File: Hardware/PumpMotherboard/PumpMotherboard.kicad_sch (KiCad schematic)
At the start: 1 part

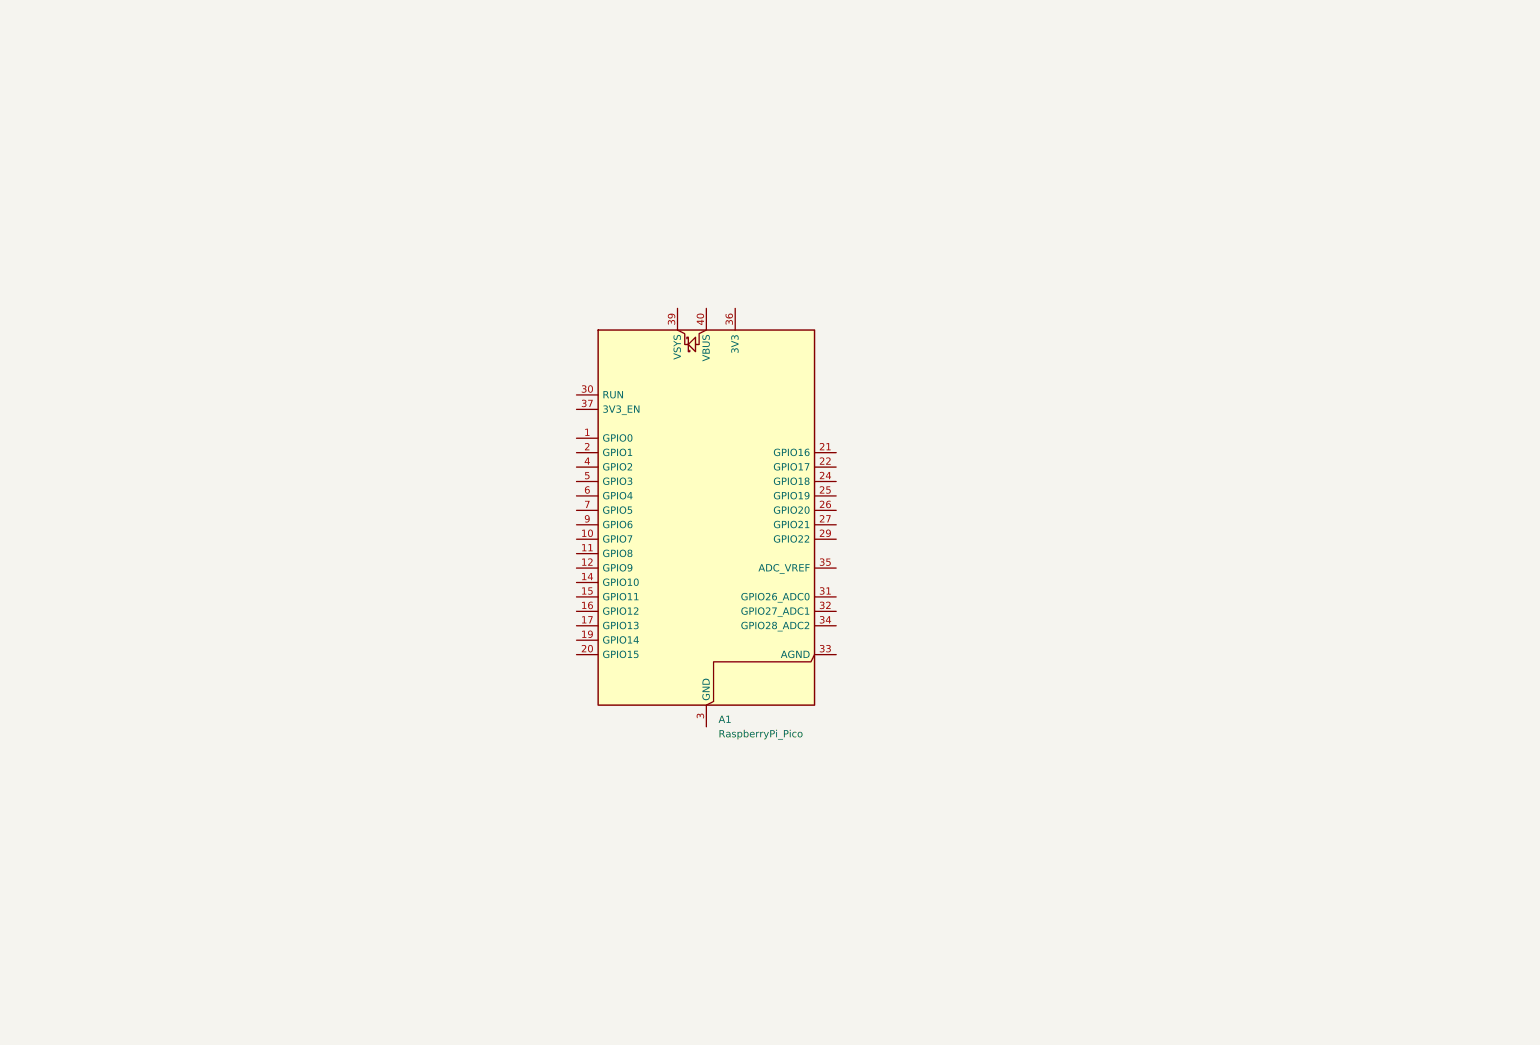
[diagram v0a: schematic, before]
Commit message: Add more bits to motherboard/controller panel
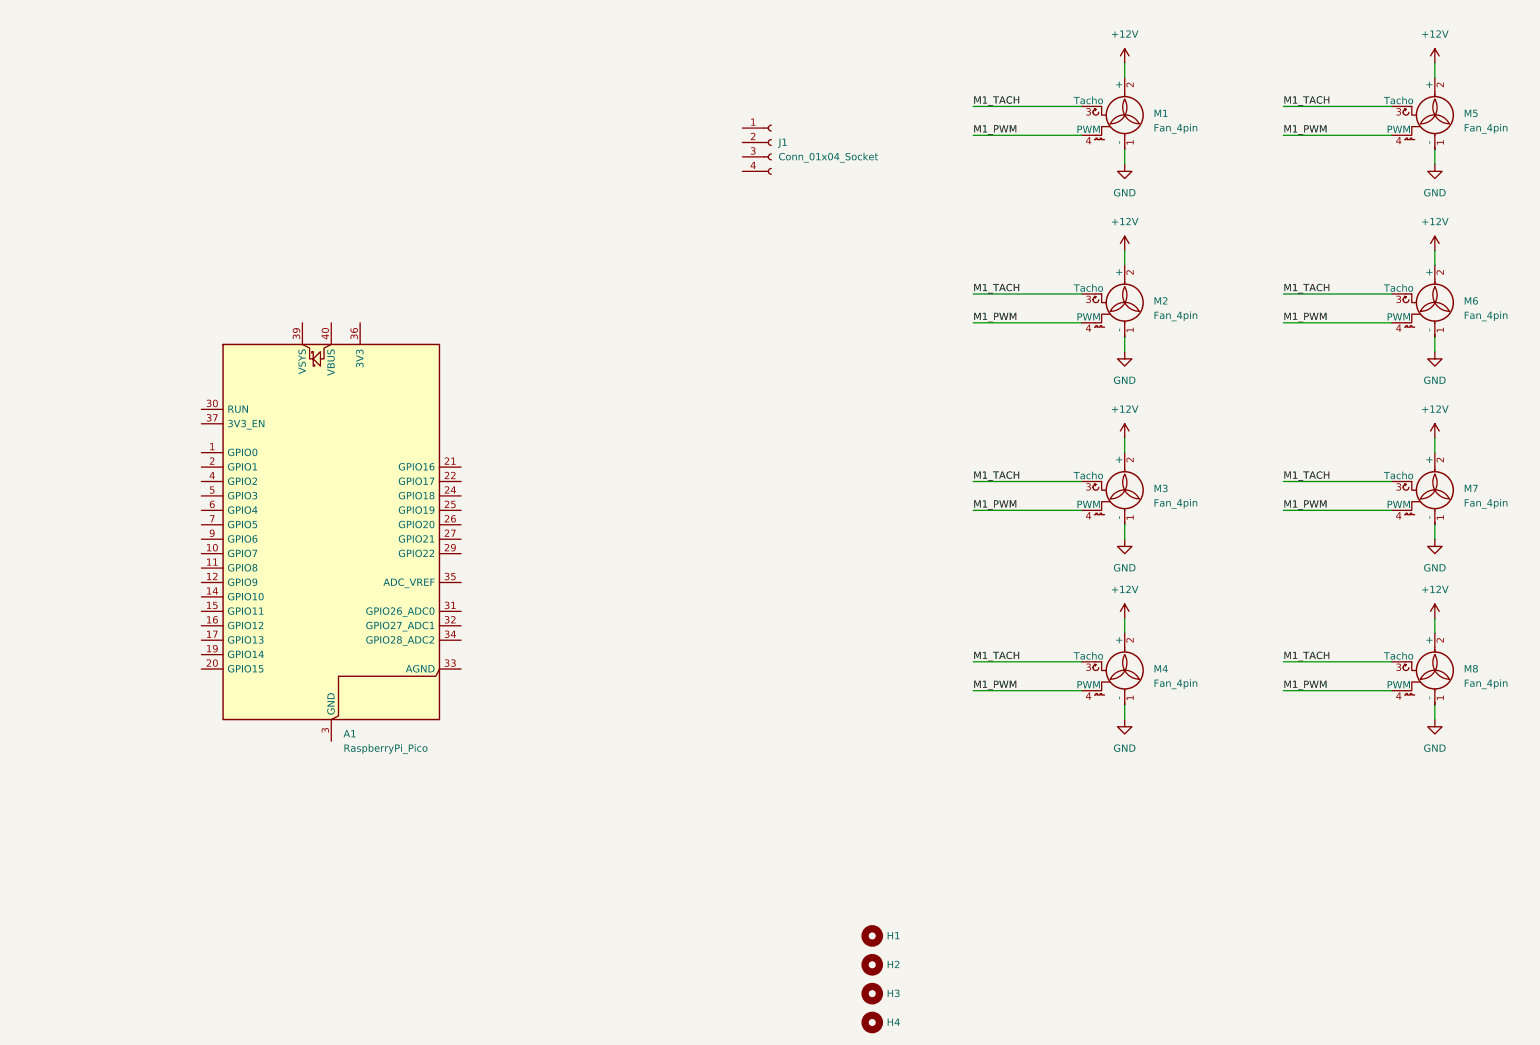
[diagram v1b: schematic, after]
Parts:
- added H1, H2, H3, H4: MountingHole, MountingHole:MountingHole_4.3mm_M4, symbol Mechanical:MountingHole
- added J1: Conn_01x04_Socket, Connector_PinSocket_2.54mm:PinSocket_1x04_P2.54mm_Vertical, symbol Connector:Conn_01x04_Socket
- added M1, M2, M3, M4, M5, M6, M7, M8: Fan_4pin, Connector:FanPinHeader_1x04_P2.54mm_Vertical, symbol Motor:Fan_4pin
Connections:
- new net +12V: M1.2 (+), M2.2 (+), M3.2 (+), M4.2 (+), M5.2 (+), M6.2 (+), M7.2 (+), M8.2 (+)
- new net GND: M1.1 (-), M2.1 (-), M3.1 (-), M4.1 (-), M5.1 (-), M6.1 (-), M7.1 (-), M8.1 (-)
- new net M1_PWM: M1.4 (PWM), M2.4 (PWM), M3.4 (PWM), M4.4 (PWM), M5.4 (PWM), M6.4 (PWM), M7.4 (PWM), M8.4 (PWM)
- new net M1_TACH: M1.3 (Tacho), M2.3 (Tacho), M3.3 (Tacho), M4.3 (Tacho), M5.3 (Tacho), M6.3 (Tacho), M7.3 (Tacho), M8.3 (Tacho)
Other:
- moved on the sheet: A1

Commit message: Replicate plugin is being a pain
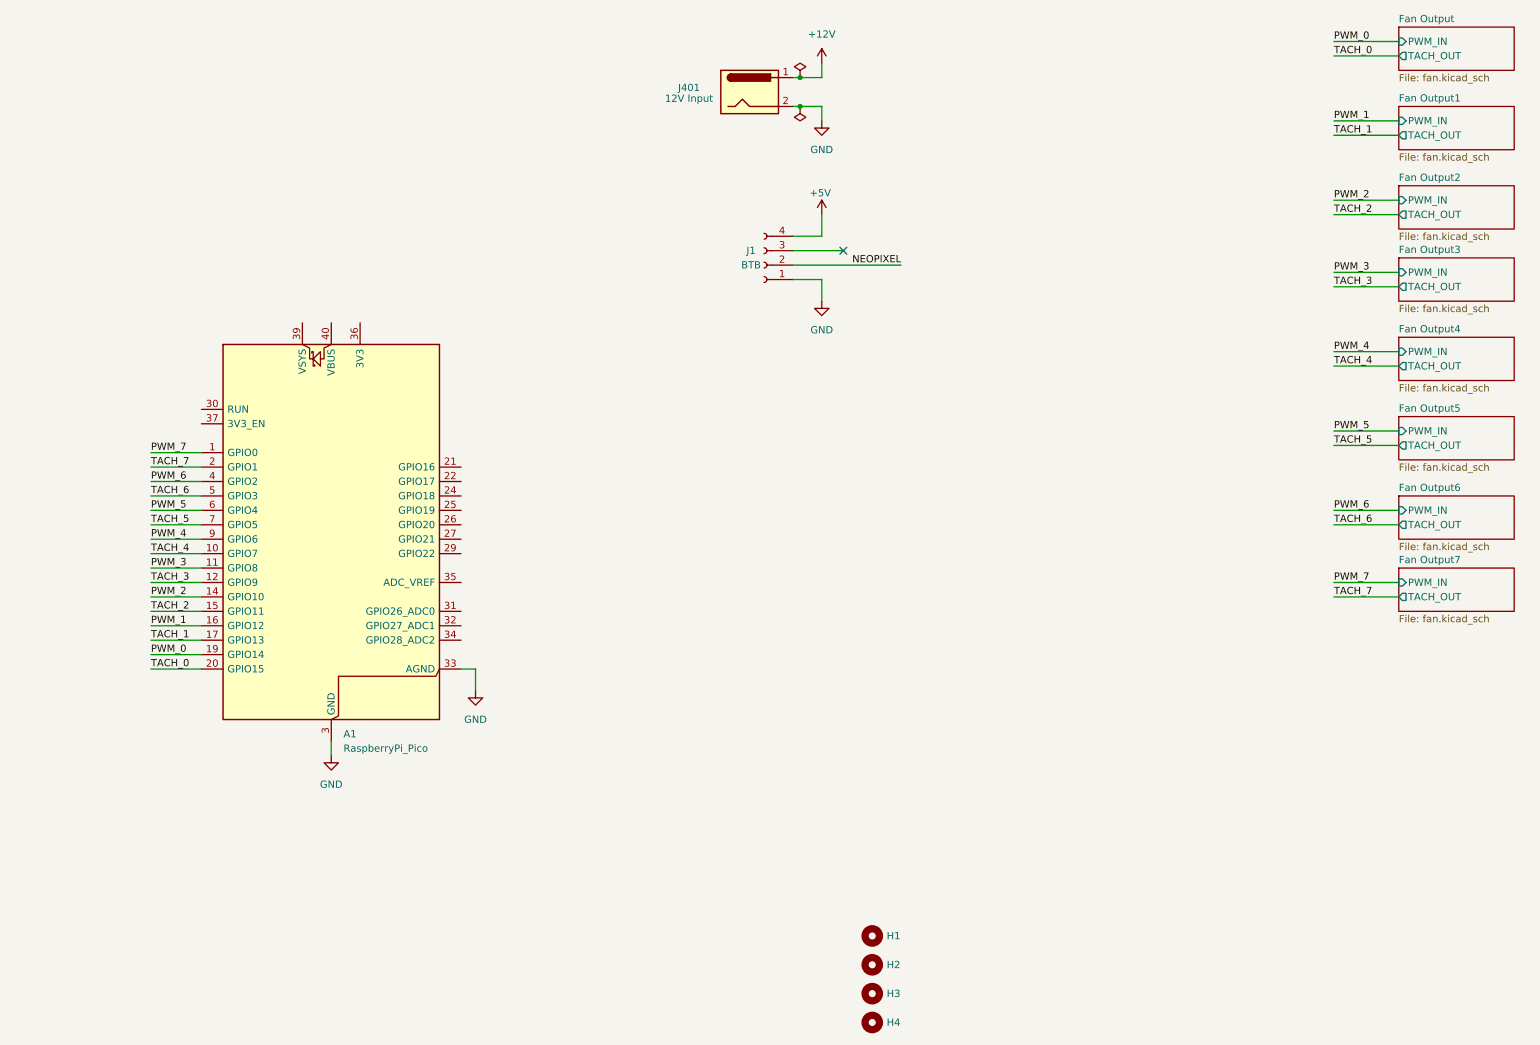
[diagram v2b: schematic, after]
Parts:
- removed M1, M2, M3, M4, M5, M6, M7, M8: Fan_4pin, Connector:FanPinHeader_1x04_P2.54mm_Vertical, symbol Motor:Fan_4pin
- added J401: 12V Input, Connector_BarrelJack:BarrelJack_GCT_DCJ200-10-A_Horizontal, symbol Connector:Barrel_Jack
- J1: value Conn_01x04_Socket -> BTB
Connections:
- net +12V: now also J401.1
- net GND: now also A1.13 (GND), A1.18 (GND), A1.23 (GND), A1.28 (GND), A1.3 (GND), A1.33 (AGND), A1.38 (GND), A1.8 (GND), J1.1 (Pin_1), J401.2
- net PWM_7: now reaches A1.1 (GPIO0)
- net TACH_4: now reaches A1.10 (GPIO7)
- net PWM_3: now reaches A1.11 (GPIO8)
- net TACH_3: now reaches A1.12 (GPIO9)
- net PWM_2: now reaches A1.14 (GPIO10)
- net TACH_2: now reaches A1.15 (GPIO11)
- net PWM_1: now reaches A1.16 (GPIO12)
- net TACH_1: now reaches A1.17 (GPIO13)
- net PWM_0: now reaches A1.19 (GPIO14)
- net TACH_7: now reaches A1.2 (GPIO1)
- net TACH_0: now reaches A1.20 (GPIO15)
- net PWM_6: now reaches A1.4 (GPIO2)
- net TACH_6: now reaches A1.5 (GPIO3)
- net PWM_5: now reaches A1.6 (GPIO4)
- net TACH_5: now reaches A1.7 (GPIO5)
- net PWM_4: now reaches A1.9 (GPIO6)
- net NEOPIXEL: now reaches J1.2 (Pin_2)
- net +5V: now reaches J1.4 (Pin_4)
- no-connect marks 0 -> 1
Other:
- added sheet Fan Output (fan.kicad_sch)
- added sheet Fan Output1 (fan.kicad_sch)
- added sheet Fan Output2 (fan.kicad_sch)
- added sheet Fan Output3 (fan.kicad_sch)
- added sheet Fan Output4 (fan.kicad_sch)
- added sheet Fan Output5 (fan.kicad_sch)
- added sheet Fan Output6 (fan.kicad_sch)
- added sheet Fan Output7 (fan.kicad_sch)
- moved on the sheet: J1

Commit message: Add tsensors, misc bits
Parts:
- added C1: 10uF, Capacitor_SMD:CP_Elec_4x3, symbol Device:C_Polarized
- added C2: 100nF, Capacitor_SMD:C_0805_2012Metric, symbol Device:C_Small
- added D1: PWR, LED_SMD:LED_0805_2012Metric, symbol Device:LED
- added J2: Conn_01x03_Pin, Connector_JST:JST_PH_B3B-PH-K_1x03_P2.00mm_Vertical, symbol Connector:Conn_01x03_Pin
- added L1: 4.7uH, Inductor_SMD:L_APV_ANR4012, symbol Device:L_Small
- added R17: 0R, Resistor_SMD:R_0805_2012Metric, symbol Device:R
- added R18: 1K, Resistor_SMD:R_0805_2012Metric, symbol Device:R
- added U2: AP63205WU, Package_TO_SOT_SMD:TSOT-23-6, symbol Regulator_Switching:AP63205WU
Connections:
- net +12V: now also C1.1, U2.2 (EN), U2.3 (IN)
- net +5V: now also J2.3 (Pin_3), L1.2, R18.1, U2.1 (FB)
- net GND: now also C1.2, D1.1 (K), J2.1 (Pin_1), U2.4 (GND)
- net NEOPIXEL: now also R17.2
- net at A1.21 (GPIO16): now also R17.1
- net AC_LEDS: now reaches A1.22 (GPIO17)
- net AC_LEDS: now also J2.2 (Pin_2)
- net TSENSOR_0: now reaches A1.31 (GPIO26_ADC0)
- net TSENSOR_1: now reaches A1.32 (GPIO27_ADC1)
- net TSENSOR_2: now reaches A1.34 (GPIO28_ADC2)
- net +3V3: now reaches A1.36 (3V3)
- new net: D1.2 (A), R18.2
- new net: C2.2, L1.1, U2.5 (SW)
- new net: C2.1, U2.6 (BST)
- no-connect marks 1 -> 8
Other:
- added sheet NTC Sensor (ntc.kicad_sch)
- added sheet NTC Sensor1 (ntc.kicad_sch)
- added sheet NTC Sensor2 (ntc.kicad_sch)
- moved on the sheet: A1, J1, J401

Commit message: Fix DRC and ERC and add AGND
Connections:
- net +5V: now also A1.39 (VSYS)
- net GND: no longer A1.33 (AGND)
- new net GNDA: A1.33 (AGND)
- no-connect marks 8 -> 10
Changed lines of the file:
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@@
 	)
 	(junction
-		(at 224.79 31.75)
-		(diameter 0)
-		(color 0 0 0 0)
-	)
-	(junction
 		(at 105.41 52.07)
 		(diameter 0)
@@
 	)
 	(no_connect
+		(at 107.95 118.11)
+	)
+	(no_connect
 		(at 153.67 138.43)
 	)
@@
 	)
 	(no_connect
+		(at 107.95 115.57)
+	)
+	(no_connect
 		(at 153.67 130.81)
 	)
@@
 	(wire
 		(pts
-			(xy 224.79 31.75) (xy 223.52 31.75)
-		)
-		(stroke
-			(width 0)
-			(type default)
-		)
-	)
-	(wire
-		(pts
 			(xy 250.19 63.5) (xy 261.62 63.5)
 		)
@@
 	(wire
 		(pts
-			(xy 228.6 31.75) (xy 224.79 31.75)
+			(xy 223.52 31.75) (xy 228.6 31.75)
 		)
 		(stroke
@@
 	(wire
 		(pts
-			(xy 156.21 161.29) (xy 156.21 165.1)
-		)
-		(stroke
-			(width 0)
-			(type default)
-		)
-	)
-	(wire
-		(pts
 			(xy 101.6 52.07) (xy 105.41 52.07)
 		)
@@
 	(wire
 		(pts
-			(xy 156.21 161.29) (xy 153.67 161.29)
-		)
-		(stroke
-			(width 0)
-			(type default)
-		)
-	)
-	(wire
-		(pts
 			(xy 115.57 46.99) (xy 115.57 52.07)
 		)
@@
 	(wire
 		(pts
+			(xy 160.02 161.29) (xy 153.67 161.29)
+		)
+		(stroke
+			(width 0)
+			(type default)
+		)
+	)
+	(wire
+		(pts
+			(xy 160.02 176.53) (xy 160.02 161.29)
+		)
+		(stroke
+			(width 0)
+			(type default)
+		)
+	)
+	(wire
+		(pts
 			(xy 99.06 153.67) (xy 107.95 153.67)
 		)
@@
 	)
 	(symbol
+		(lib_id "power:+5V")
+		(at 125.73 96.52 0)
+		(unit 1)
+		(body_style 1)
+		(exclude_from_sim no)
+		(in_bom yes)
+		(on_board yes)
+		(in_pos_files yes)
+		(dnp no)
+		(fields_autoplaced yes)
+		(property "Reference" "#PWR053"
+			(at 125.73 100.33 0)
+			(hide yes)
+			(show_name no)
+			(do_not_autoplace no)
+			(effects
+				(font
+					(size 1.27 1.27)
+				)
+			)
+		)
+		(property "Value" "+5V"
+			(at 125.73 91.44 0)
+			(show_name no)
+			(do_not_autoplace no)
+			(effects
+				(font
+					(size 1.27 1.27)
+				)
+			)
+		)
+		(property "Footprint" ""
+			(at 125.73 96.52 0)
+			(hide yes)
+			(show_name no)
+			(do_not_autoplace no)
+			(effects
+				(font
+					(size 1.27 1.27)
+				)
+			)
+		)
+		(property "Datasheet" ""
+			(at 125.73 96.52 0)
+			(hide yes)
+			(show_name no)
+			(do_not_autoplace no)
+			(effects
+				(font
+					(size 1.27 1.27)
+				)
+			)
+		)
+		(property "Description" "Power symbol creates a global label with name \"+5V\""
+			(at 125.73 96.52 0)
+			(hide yes)
+			(show_name no)
+			(do_not_autoplace no)
+			(effects
+				(font
+					(size 1.27 1.27)
+				)
+			)
+		)
+		(pin "1"
+		)
+		(instances
+			(project "PumpMotherboard"
+				(path "/0d3b5c69-c1f2-4eab-9f51-de1d9dac9894"
+					(reference "#PWR053")
+					(unit 1)
+				)
+			)
+		)
+	)
+	(symbol
 		(lib_id "Device:C_Polarized")
 		(at 40.64 55.88 0)
@@
 	)
 	(symbol
-		(lib_id "power:PWR_FLAG")
-		(at 224.79 31.75 180)
+		(lib_id "power:GNDA")
+		(at 160.02 176.53 0)
 		(unit 1)
 		(body_style 1)
@@
 		(dnp no)
 		(fields_autoplaced yes)
-		(property "Reference" "#FLG02"
-			(at 224.79 33.655 0)
+		(property "Reference" "#PWR018"
+			(at 160.02 182.88 0)
 			(hide yes)
 			(show_name no)
@@
 			)
 		)
-		(property "Value" "PWR_FLAG"
-			(at 224.79 36.83 0)
-			(hide yes)
+		(property "Value" "GNDA"
+			(at 160.02 181.61 0)
 			(show_name no)
 			(do_not_autoplace no)
@@
 		)
 		(property "Footprint" ""
-			(at 224.79 31.75 0)
+			(at 160.02 176.53 0)
 			(hide yes)
 			(show_name no)
@@
 		)
 		(property "Datasheet" ""
-			(at 224.79 31.75 0)
+			(at 160.02 176.53 0)
 			(hide yes)
 			(show_name no)
@@
 			)
 		)
-		(property "Description" "Special symbol for telling ERC where power comes from"
-			(at 224.79 31.75 0)
+		(property "Description" "Power symbol creates a global label with name \"GNDA\" , analog ground"
+			(at 160.02 176.53 0)
 			(hide yes)
 			(show_name no)
@@
 			(project "PumpMotherboard"
 				(path "/0d3b5c69-c1f2-4eab-9f51-de1d9dac9894"
-					(reference "#FLG02")
+					(reference "#PWR018")
 					(unit 1)
 				)
@@
 	)
 	(symbol
-		(lib_id "power:GND")
-		(at 156.21 165.1 0)
-		(unit 1)
-		(body_style 1)
-		(exclude_from_sim no)
-		(in_bom yes)
-		(on_board yes)
-		(in_pos_files yes)
-		(dnp no)
-		(fields_autoplaced yes)
-		(property "Reference" "#PWR018"
-			(at 156.21 171.45 0)
-			(hide yes)
-			(show_name no)
-			(do_not_autoplace no)
-			(effects
-				(font
-					(size 1.27 1.27)
-				)
-			)
-		)
-		(property "Value" "GND"
-			(at 156.21 170.18 0)
-			(show_name no)
-			(do_not_autoplace no)
-			(effects
-				(font
-					(size 1.27 1.27)
-				)
-			)
-		)
-		(property "Footprint" ""
-			(at 156.21 165.1 0)
-			(hide yes)
-			(show_name no)
-			(do_not_autoplace no)
-			(effects
-				(font
-					(size 1.27 1.27)
-				)
-			)
-		)
-		(property "Datasheet" ""
-			(at 156.21 165.1 0)
-			(hide yes)
-			(show_name no)
-			(do_not_autoplace no)
-			(effects
-				(font
-					(size 1.27 1.27)
-				)
-			)
-		)
-		(property "Description" "Power symbol creates a global label with name \"GND\" , ground"
-			(at 156.21 165.1 0)
-			(hide yes)
-			(show_name no)
-			(do_not_autoplace no)
-			(effects
-				(font
-					(size 1.27 1.27)
-				)
-			)
-		)
-		(pin "1"
-		)
-		(instances
-			(project "PumpMotherboard"
-				(path "/0d3b5c69-c1f2-4eab-9f51-de1d9dac9894"
-					(reference "#PWR018")
-					(unit 1)
-				)
-			)
-		)
-	)
-	(symbol
 		(lib_id "Device:C_Small")
 		(at 86.36 53.34 90)
@@
 			)
 		)
-		(property "Description" ""
-			(at 215.9 29.21 0)
+		(property "Description" "DC Barrel Jack"
+			(at 215.9 23.876 0)
 			(show_name no)
 			(do_not_autoplace no)

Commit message: Add LCSC part num
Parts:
- U2: LCSC# (none) -> C2071056
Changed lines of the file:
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@@
+			)
+		)
+		(property "LCSC#" "C2071056"
+			(at 68.58 53.34 0)
+			(hide yes)
+			(show_name no)
+			(do_not_autoplace no)
+			(effects
+				(font
+					(size 1.27 1.27)
+				)
 			)
 		)

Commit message: Add SW inputs
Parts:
- added J6: SW_IN0, Connector_JST:JST_XH_B2B-XH-A_1x02_P2.50mm_Vertical, symbol Connector:Conn_01x02_Pin
- added J7: SW_IN1, Connector_JST:JST_XH_B2B-XH-A_1x02_P2.50mm_Vertical, symbol Connector:Conn_01x02_Pin
- added J8: SW_IN2, Connector_JST:JST_XH_B2B-XH-A_1x02_P2.50mm_Vertical, symbol Connector:Conn_01x02_Pin
- J2: value Conn_01x03_Pin -> AC_LEDs; footprint Connector_JST:JST_PH_B3B-PH-K_1x03_P2.00mm_Vertical -> Connector_JST:JST_XH_B3B-XH-A_1x03_P2.50mm_Vertical
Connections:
- net GND: now also J6.2 (Pin_2), J7.2 (Pin_2), J8.2 (Pin_2)
- net SW_0: now reaches A1.24 (GPIO18)
- net SW_0: now also J6.1 (Pin_1)
- net SW_1: now reaches A1.25 (GPIO19)
- net SW_1: now also J7.1 (Pin_1)
- net SW_2: now reaches A1.26 (GPIO20)
- net SW_2: now also J8.1 (Pin_1)
- no-connect marks 10 -> 7
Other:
- moved on the sheet: J2

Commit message: Add 12v power switching
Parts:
- added Q10: MMBT3904, Package_TO_SOT_SMD:SOT-23, symbol Transistor_BJT:MMBT3904
- added Q9: AO4407A, Package_SO:SOIC-8_5.3x5.3mm_P1.27mm, symbol KenwoodFox:AO4407A
- added R22: 10K, Resistor_SMD:R_0805_2012Metric, symbol Device:R_Small
- added R23: 1K, Resistor_SMD:R_0805_2012Metric, symbol Device:R_Small
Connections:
- net +12V: now also Q9.1 (S), Q9.2 (S), Q9.3 (S), R22.1
- net GND: now also Q10.2 (E)
- net LOAD_EN: now reaches A1.27 (GPIO21)
- net LOAD_EN: now also R23.1
- new net: Q10.1 (B), R23.2
- new net: Q10.3 (C), Q9.4 (G), R22.2
- new net 12V_SWITCHED: Q9.5 (D), Q9.6 (D), Q9.7 (D), Q9.8 (D)
- no-connect marks 7 -> 6
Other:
- moved on the sheet: C1, C2, D1, L1, R18, U2
